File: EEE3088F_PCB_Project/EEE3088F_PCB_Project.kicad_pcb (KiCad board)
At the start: 2 copper layers, 91.6 x 148.6 mm, 107 parts, among them IC1 DRV8833PWPR, IC2 DRV8833PWPR, IC3 TPS62067DSGR, IC5 INA219AIDCNR, IC7 TPS61088RHLR, J1 Conn_02x16_Odd_Even, J2 TYPE-C16PIN, J3 Conn_01x02, Q1 AO3400A, Q2 AO3400A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

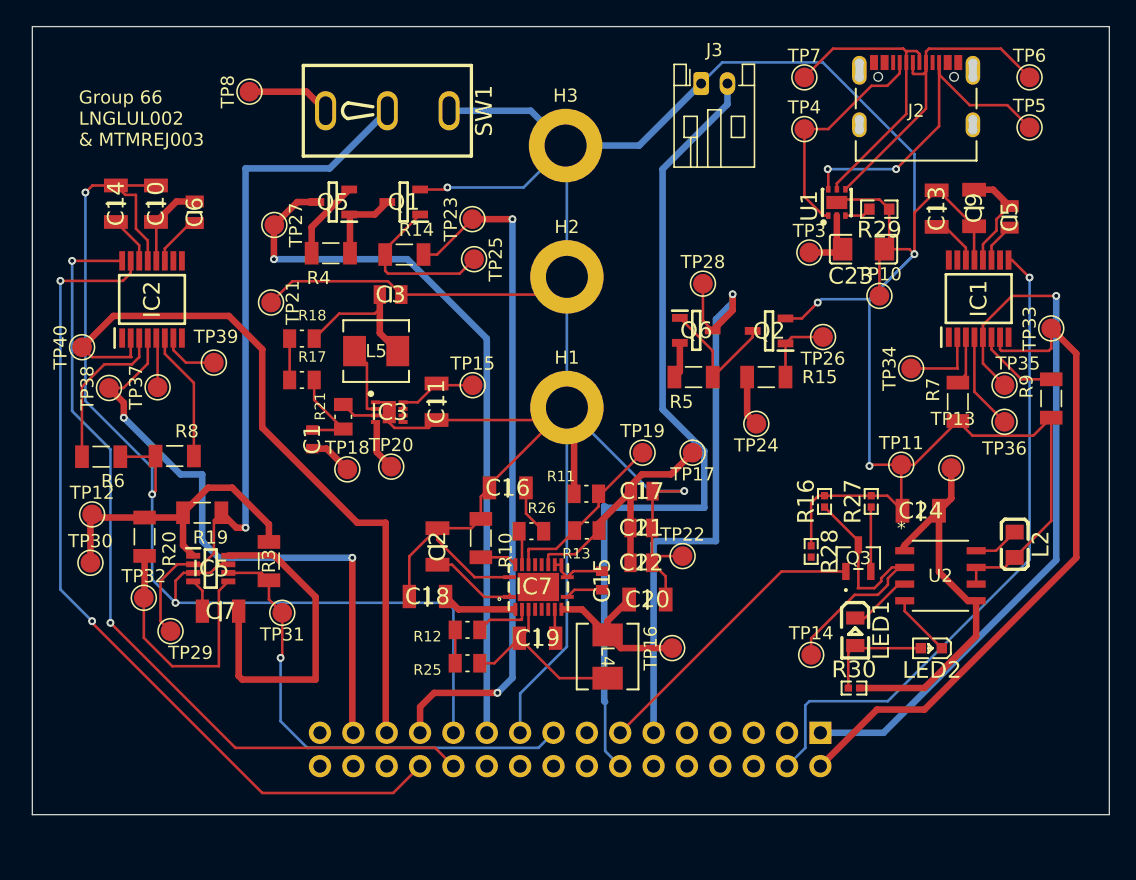
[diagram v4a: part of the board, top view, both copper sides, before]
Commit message: v1.5.5
- just need to connect motor pins
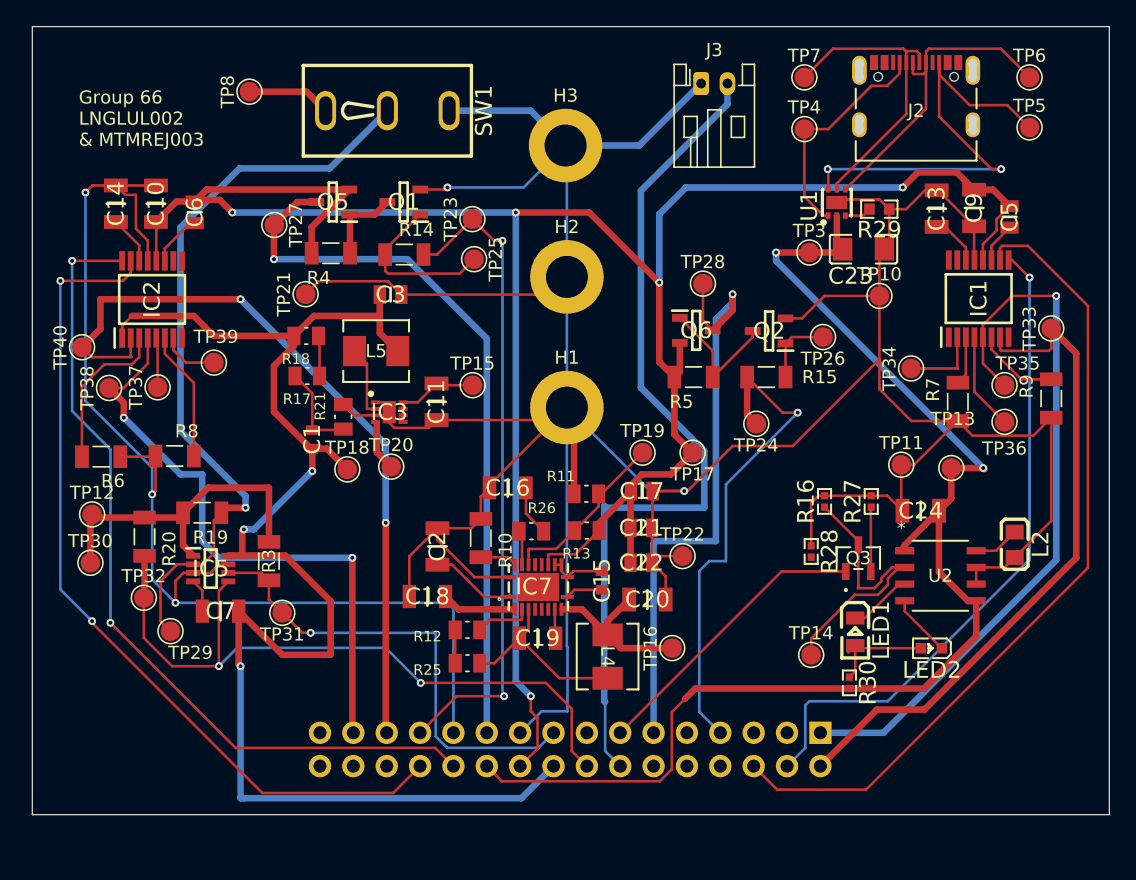
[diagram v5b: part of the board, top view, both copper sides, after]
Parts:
- moved TP21 2.71 mm to (122.7, 72.8), turned to 90 degrees
- moved R30 0.53 mm to (164.1, 102.4), turned to -90 degrees
- moved R17 0.51 mm to (122.8, 79.0), turned to 180 degrees
- moved R18 0.39 mm to (122.7, 75.9), turned to 180 degrees
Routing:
- net /5V OUT: track 44.8 -> 183.3 mm, vias 0 -> 5
- net /3V3 OUT: track 40.3 -> 113.5 mm, vias 0 -> 3
- net /MOTOR2_CTRL2: track 0.00 -> 62.7 mm
- net /HV: track 34.6 -> 97.1 mm, vias 0 -> 2
- net /I2C1_SCL: track 20.0 -> 54.2 mm, vias 0 -> 2
- net /CTRL_EXT_LOAD2: track 3.85 -> 37.7 mm, vias 0 -> 1
- net GND: track 413.9 -> 388.9 mm, vias 8 -> 5
- net /CC2: track 25.7 -> 34.7 mm
- net /BATTERY: track 87.9 -> 90.9 mm
- net /CTRL_EXT_LOAD1: track 52.7 -> 50.1 mm
- net /PWR SWITCH IN: track 54.7 -> 57.2 mm
- net /MOTOR3_A_OUT: track 55.7 -> 58.1 mm, vias 0 -> 2

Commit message: v1.5.6
- 4 more main connectors to go
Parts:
- moved TP24 4.94 mm to (161.7, 81.0)
- moved TP31 0.77 mm to (120.1, 97.2)
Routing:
- net /MOTOR1_CTRL2: track 0.00 -> 103.9 mm, vias 0 -> 1
- net /MOTOR1_CTRL1: track 0.00 -> 94.7 mm, vias 0 -> 1
- net /BATTERY: track 90.9 -> 172.2 mm, vias 0 -> 1
- net /MOTOR1_A_OUT: track 5.95 -> 85.5 mm, vias 0 -> 3
- net /MOTOR1_B_OUT: track 7.50 -> 83.6 mm, vias 0 -> 2
- net /5V OUT: track 183.3 -> 196.2 mm, vias 5 -> 7
- net /HV: track 97.1 -> 109.3 mm
- net /PWR SWITCH IN: track 57.2 -> 65.9 mm, vias 1 -> 2
- net /3V3 OUT: track 113.5 -> 108.4 mm
- net GND: track 388.9 -> 384.1 mm
- net /CTRL_EXT_LOAD2: track 37.7 -> 39.7 mm
- net /I2C1_SDA: track 36.2 -> 34.3 mm
- net /MOTOR3_A_OUT: track 58.1 -> 59.4 mm
- net /MOTOR2_CTRL1: track 50.5 -> 51.1 mm
- net /FAST_CHARGE_CTRL: track 22.3 -> 22.9 mm
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
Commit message: v1.6
- all wiring done!
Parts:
- moved TP15 3.83 mm to (132.9, 76.8)
- moved R25 2.36 mm to (133.3, 99.2), turned to -90 degrees
- moved TP18 2.03 mm to (125.5, 88.1)
- moved R10 1.82 mm to (135.8, 89.5)
- moved TP28 1.68 mm to (154.1, 70.8)
- moved C16 1.51 mm to (139.6, 87.6)
- moved R5 1.28 mm to (152.3, 77.8)
- moved Q6 1.28 mm to (152.5, 74.2)
- moved R12 1.21 mm to (136.1, 97.9), turned to -90 degrees
- moved LED2 0.94 mm to (169.4, 99.4)
- moved TP20 0.82 mm to (128.4, 85.7)
- moved TP19 0.57 mm to (147.8, 85.1)
- moved C2 0.55 mm to (133.1, 91.6)
- moved C18 0.38 mm to (132.2, 95.5)
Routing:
- net /MOTOR4_CTRL2: track 0.00 -> 98.5 mm, vias 0 -> 4
- net /MOTOR4_CTRL1: track 0.00 -> 98.0 mm, vias 0 -> 4
- net /MOTOR4_A_OUT: track 4.39 -> 92.5 mm, vias 0 -> 1
- net /MOTOR4_B_OUT: track 3.79 -> 81.2 mm, vias 0 -> 1
- net /3V3 OUT: track 108.4 -> 157.0 mm, vias 3 -> 5
- net /BATTERY: track 172.2 -> 163.0 mm, vias 1 -> 2
- net GND: track 384.1 -> 379.4 mm, vias 5 -> 9
- net Net-(IC2-BISEN): track 9.90 -> 13.6 mm
- net /MOTOR2_CTRL1: track 51.1 -> 47.6 mm
- net /MOTOR1_B_OUT: track 83.6 -> 87.0 mm
- net /MOTOR1_A_OUT: track 85.5 -> 88.6 mm
- net /EXT_LOAD1_OUT: track 55.3 -> 58.4 mm
- net /MOTOR2_B_OUT: track 55.4 -> 52.6 mm
- net Net-(IC3-FB): track 11.0 -> 13.4 mm
- net Net-(IC7-SW_1): track 14.4 -> 16.6 mm
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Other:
- board size 91.6 x 148.6 mm -> 82 x 60 mm
